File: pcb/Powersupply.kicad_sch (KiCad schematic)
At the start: 20 parts, among them IC3 UCC28910DR

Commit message: minor corrections
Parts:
- removed C15: 100p, Capacitor_SMD:C_0201_0603Metric, symbol Device:C
- removed R25: 1k3, Resistor_SMD:R_0201_0603Metric, symbol Device:R
- added R27: 1M, Resistor_SMD:R_0201_0603Metric, symbol Device:R
- C12: value 220p -> 470n
- C13: value 0.1u -> 100n
- C14: value 100u -> 47u
- C17: value 100p -> 100n
- C19: value 470u -> 1m
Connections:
- net RECT+: now also R27.1
- net RECT-: now also R27.2
- net at IC3.4 (IPK): now also C14.2, C17.2, D9.1 (K), IC3.1 (GND_1), IC3.2 (GND_2), IC3.3 (GND_3), L1.1, R23.2
- net at C13.1, C19.1, D10.2 (A)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: no longer C14.1, C17.1
- net at D10.1 (K), IC3.6 (VDD): now also C14.1, C17.1
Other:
- note added: "auto max current"
- moved on the sheet: C12, C13, C14, C17, C19, D10, D8, D9, IC3, JP10, JP9, L1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

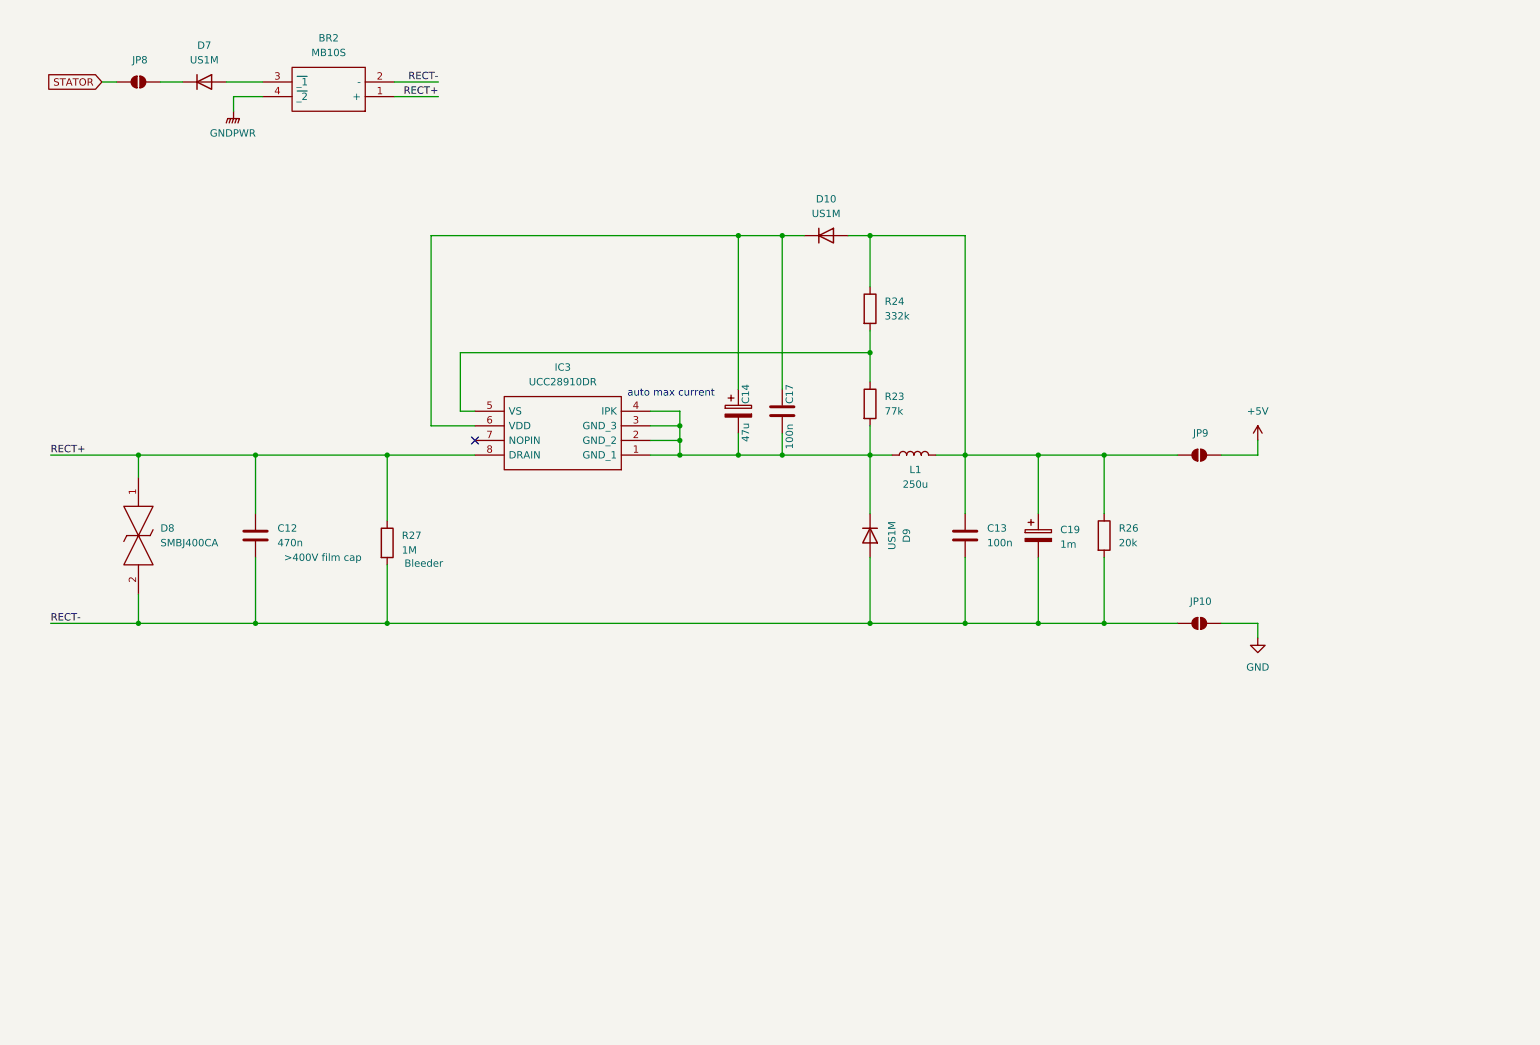
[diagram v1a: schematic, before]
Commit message: added predisposition for second piezo conditioning circuit
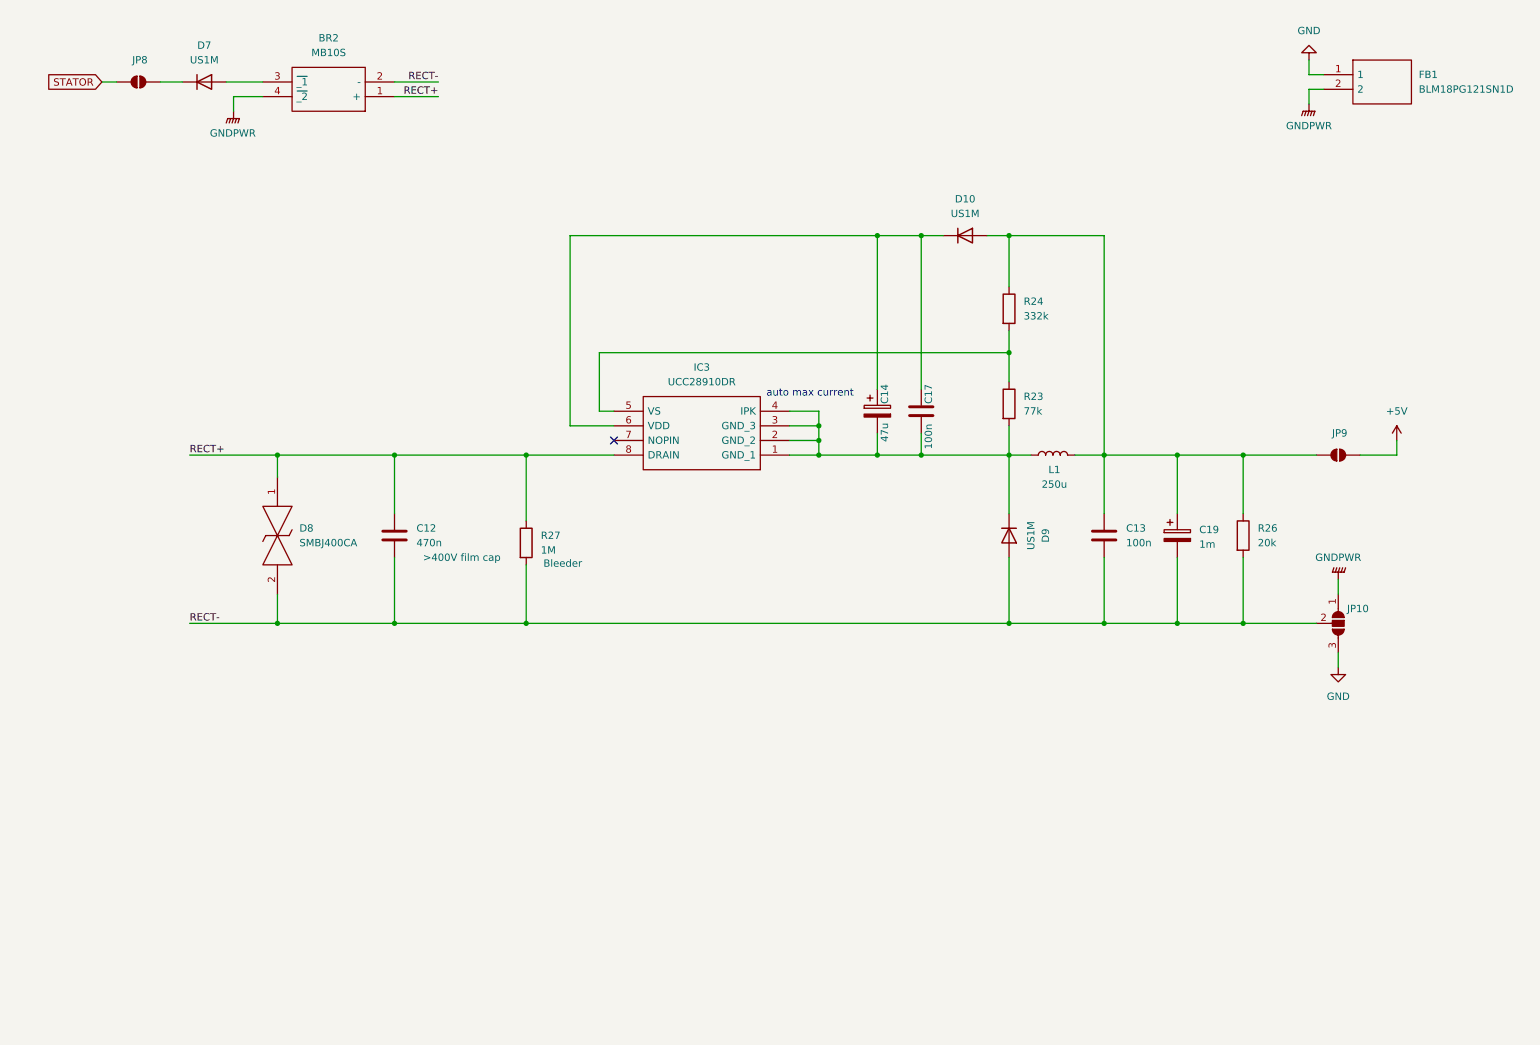
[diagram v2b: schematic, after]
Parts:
- removed JP10: SolderJumper_2_Open, Jumper:SolderJumper-2_P1.3mm_Open_RoundedPad1.0x1.5mm, symbol Jumper:SolderJumper_2_Open
- added FB1: BLM18PG121SN1D, BLM18SP221SN1B, symbol SamacSys_Parts:BLM18PG121SN1D
- added JP10: SolderJumper_3_Open, Jumper:SolderJumper-3_P1.3mm_Open_RoundedPad1.0x1.5mm, symbol Jumper:SolderJumper_3_Open
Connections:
- net GND: now also FB1.1, JP10.3 (B)
- net GNDPWR: now also FB1.2, JP10.1 (A)
- net RECT-: now also JP10.2 (C)
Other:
- moved on the sheet: C12, C13, C14, C17, C19, D10, D8, D9, IC3, JP9, L1, R23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

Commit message: video call revision
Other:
- note added: "Aggiungere filtro PiGreco usare calcolatore online"
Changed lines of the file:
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@@
+		)
+	)
+	(text "Aggiungere filtro PiGreco\nusare calcolatore online\n"
+		(exclude_from_sim no)
+		(at 84.836 90.17 0)
+		(effects
+			(font
+				(size 1.27 1.27)
+			)
 		)
 	)

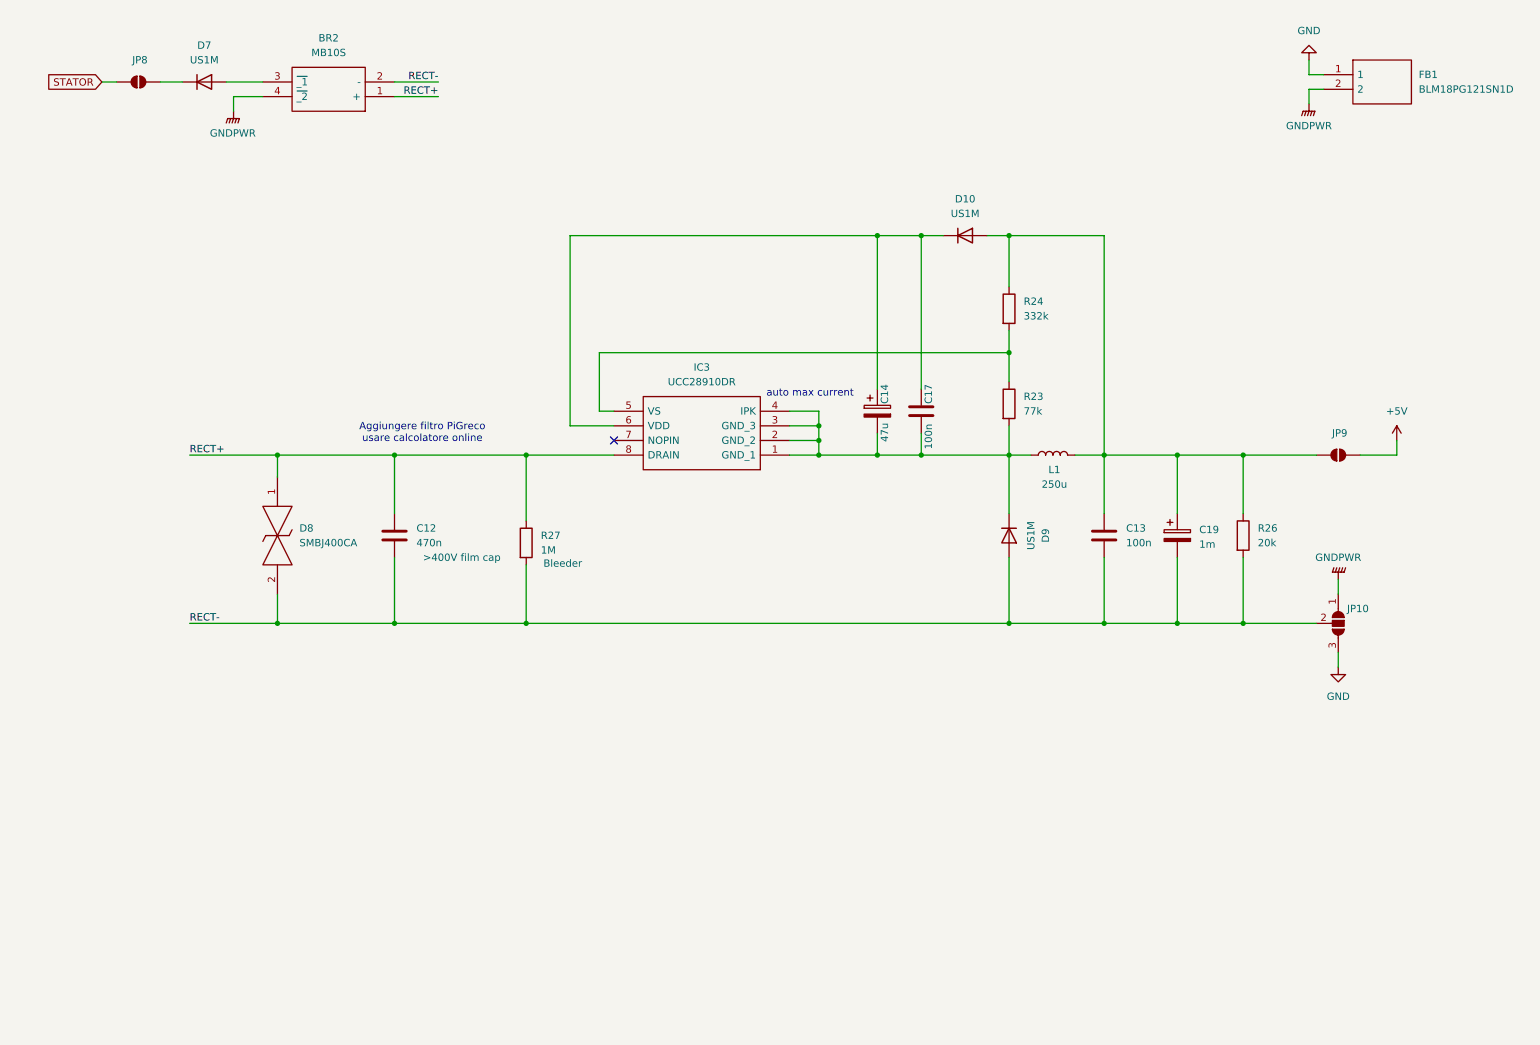
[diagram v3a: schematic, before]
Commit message: added 12 to 5 buck
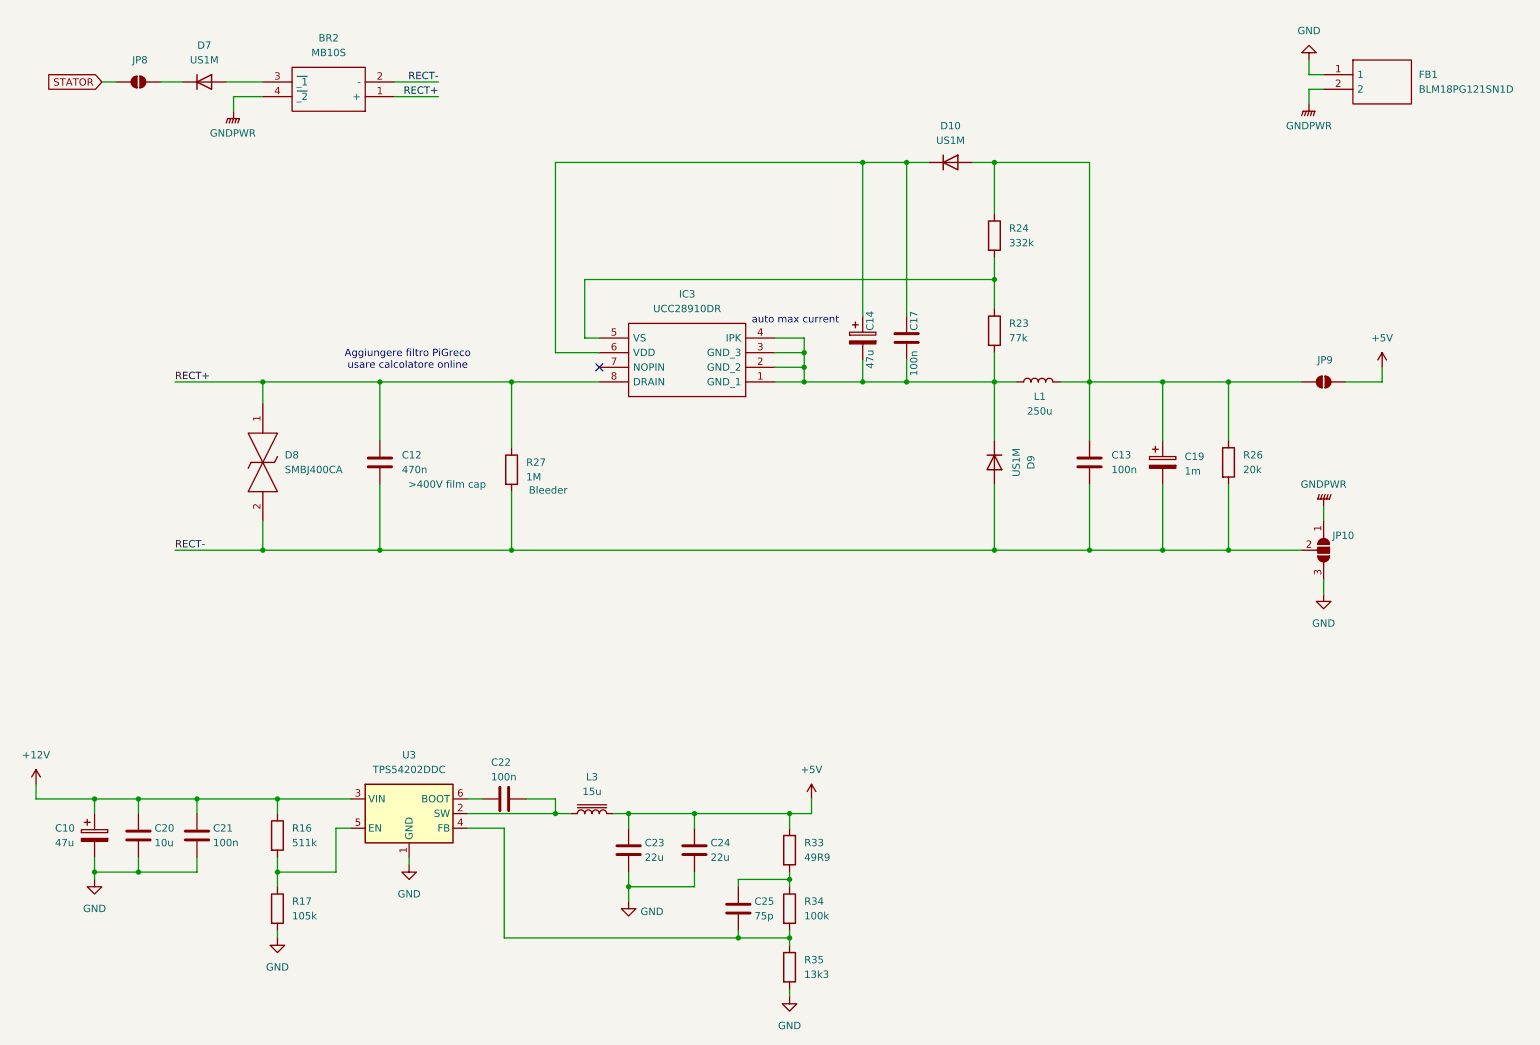
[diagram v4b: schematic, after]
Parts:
- added C10: 47u, Capacitor_SMD:CP_Elec_3x5.4, symbol Device:C_Polarized
- added C20: 10u, Capacitor_SMD:C_0201_0603Metric, symbol Device:C
- added C21, C22: 100n, Capacitor_SMD:C_0201_0603Metric, symbol Device:C
- added C23, C24: 22u, Capacitor_SMD:C_0201_0603Metric, symbol Device:C
- added C25: 75p, Capacitor_SMD:C_0201_0603Metric, symbol Device:C
- added L3: 15u, symbol Device:L_Iron
- added R16: 511k, Resistor_SMD:R_0201_0603Metric, symbol Device:R
- added R17: 105k, Resistor_SMD:R_0201_0603Metric, symbol Device:R
- added R33: 49R9, Resistor_SMD:R_0201_0603Metric, symbol Device:R
- added R34: 100k, Resistor_SMD:R_0201_0603Metric, symbol Device:R
- added R35: 13k3, Resistor_SMD:R_0201_0603Metric, symbol Device:R
- added U3: TPS54202DDC, Package_TO_SOT_SMD:SOT-23-6, symbol Regulator_Switching:TPS54202DDC
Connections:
- net +5V: now also C23.1, C24.1, L3.2, R33.1
- net GND: now also C10.2, C20.2, C21.2, C23.2, C24.2, R17.2, R35.2, U3.1 (GND)
- new net: C22.2, L3.1, U3.2 (SW)
- new net: C25.2, R34.2, R35.1, U3.4 (FB)
- new net: R16.2, R17.1, U3.5 (EN)
- new net: C22.1, U3.6 (BOOT)
- new net: C25.1, R33.2, R34.1
- new net +12V: C10.1, C20.1, C21.1, R16.1, U3.3 (VIN)
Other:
- moved on the sheet: C12, C13, C14, C17, C19, D10, D8, D9, IC3, JP10, JP9, L1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

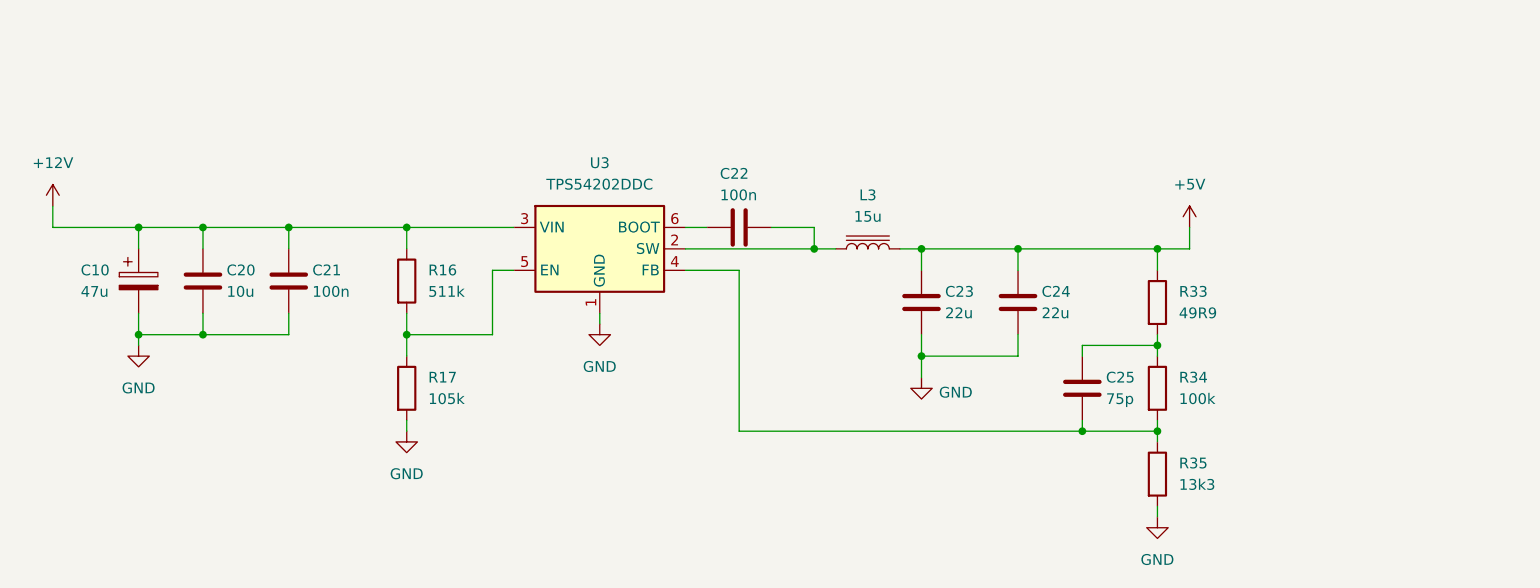
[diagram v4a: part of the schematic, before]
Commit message: added reverse polarity protection
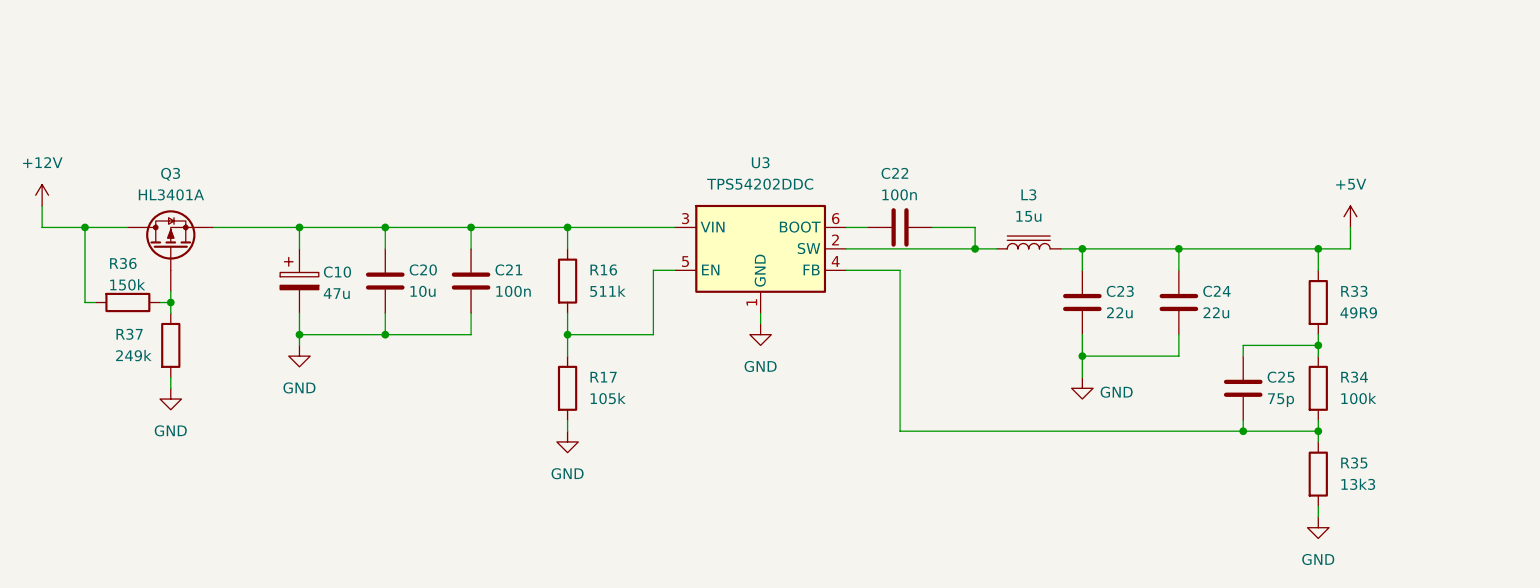
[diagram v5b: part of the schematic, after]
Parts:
- added Q3: HL3401A, symbol Device:Q_PMOS
- added R36: 150k, Resistor_SMD:R_0201_0603Metric, symbol Device:R
- added R37: 249k, Resistor_SMD:R_0201_0603Metric, symbol Device:R
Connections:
- net +12V: now also Q3.D, R36.2; no longer C10.1, C20.1, C21.1, R16.1, U3.3 (VIN)
- net GND: now also R37.2
- new net: Q3.G, R36.1, R37.1
- new net: C10.1, C20.1, C21.1, Q3.S, R16.1, U3.3 (VIN)
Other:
- moved on the sheet: C10, C20, C21, C22, C23, C24, C25, L3, R16, R17, R33, R34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
